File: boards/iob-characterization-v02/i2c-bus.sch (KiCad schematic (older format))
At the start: 14 parts, among them U13 24LC16BT, U14 PCA9306, U15 MCP4726A0, U16 MCP4726A1, U17 LTC2451

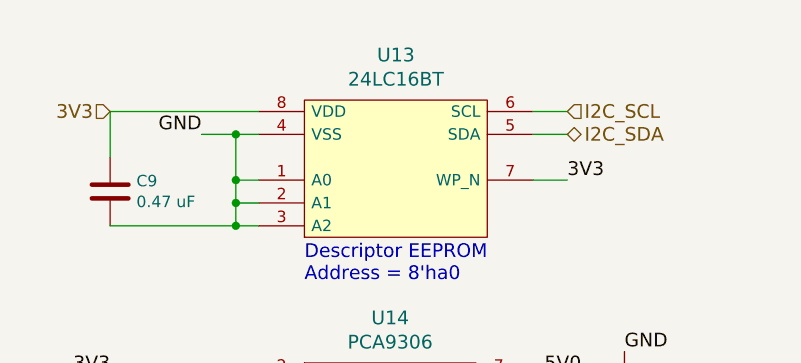
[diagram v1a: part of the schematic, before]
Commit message: Continued work on I/O characterization schematic
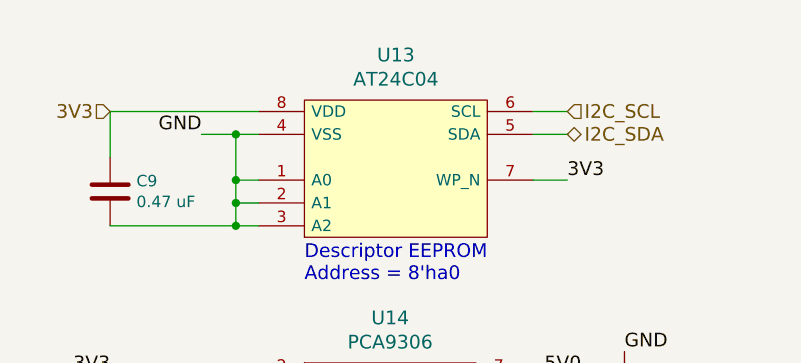
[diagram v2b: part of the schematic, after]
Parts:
- C10, C11, C13, C14, C9: footprint (none) -> azonenberg_pcb:EIA_0402_CAP_NOSILK
- R13, R14: footprint (none) -> azonenberg_pcb:EIA_0402_RES_NOSILK
- U13: value 24LC16BT -> AT24C04; footprint (none) -> azonenberg_pcb:DFN_8_0.5MM_2x3MM
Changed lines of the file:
@@
 Sheet 6 6
 Title "STARSHIPRAIDER I/O Characterization"
-Date "2018-08-10"
+Date "2018-08-13"
 Rev "0.2"
 Comp "Andrew D. Zonenberg"
@@
 AR Path="/5B92BCA2/5B932A67" Ref="U13"  Part="1"
 F 0 "U13" H 3750 3497 60  0000 C CNN
-F 1 "24LC16BT" H 3750 3391 60  0000 C CNN
-F 2 "" H 3750 3000 60  0001 C CNN
+F 1 "AT24C04" H 3750 3391 60  0000 C CNN
+F 2 "azonenberg_pcb:DFN_8_0.5MM_2x3MM" H 3750 3000 60  0001 C CNN
 F 3 "" H 3750 3000 60  0000 C CNN
 	1    3350 2700
@@
 F 0 "C9" H 2615 2546 50  0000 L CNN
 F 1 "0.47 uF" H 2615 2455 50  0000 L CNN
-F 2 "" H 2538 2350 50  0001 C CNN
+F 2 "azonenberg_pcb:EIA_0402_CAP_NOSILK" H 2538 2350 50  0001 C CNN
 F 3 "" H 2500 2500 50  0000 C CNN
 	1    2500 2500
@@
 F 0 "C11" H 4865 3396 50  0000 L CNN
 F 1 "0.47 uF" H 4865 3305 50  0000 L CNN
-F 2 "" H 4788 3200 50  0001 C CNN
+F 2 "azonenberg_pcb:EIA_0402_CAP_NOSILK" H 4788 3200 50  0001 C CNN
 F 3 "" H 4750 3350 50  0000 C CNN
 	1    4750 3350
@@
 F 0 "C10" H 2615 3496 50  0000 L CNN
 F 1 "0.47 uF" H 2615 3405 50  0000 L CNN
-F 2 "" H 2538 3300 50  0001 C CNN
+F 2 "azonenberg_pcb:EIA_0402_CAP_NOSILK" H 2538 3300 50  0001 C CNN
 F 3 "" H 2500 3450 50  0000 C CNN
 	1    2500 3450
@@
 F 0 "C13" H 7465 2346 50  0000 L CNN
 F 1 "0.47 uF" H 7465 2255 50  0000 L CNN
-F 2 "" H 7388 2150 50  0001 C CNN
+F 2 "azonenberg_pcb:EIA_0402_CAP_NOSILK" H 7388 2150 50  0001 C CNN
 F 3 "" H 7350 2300 50  0000 C CNN
 	1    7350 2300
@@
 F 0 "R13" H 5470 3596 50  0000 L CNN
 F 1 "4.7K" V 5400 3450 50  0000 L CNN
-F 2 "" V 5330 3550 50  0001 C CNN
+F 2 "azonenberg_pcb:EIA_0402_RES_NOSILK" V 5330 3550 50  0001 C CNN
 F 3 "" H 5400 3550 50  0000 C CNN
 	1    5400 3550
@@
 F 0 "R14" H 5770 3696 50  0000 L CNN
 F 1 "4.7K" V 5700 3550 50  0000 L CNN
-F 2 "" V 5630 3650 50  0001 C CNN
+F 2 "azonenberg_pcb:EIA_0402_RES_NOSILK" V 5630 3650 50  0001 C CNN
 F 3 "" H 5700 3650 50  0000 C CNN
 	1    5700 3650
@@
 F 0 "C14" H 7465 3796 50  0000 L CNN
 F 1 "0.47 uF" H 7465 3705 50  0000 L CNN
-F 2 "" H 7388 3600 50  0001 C CNN
+F 2 "azonenberg_pcb:EIA_0402_CAP_NOSILK" H 7388 3600 50  0001 C CNN
 F 3 "" H 7350 3750 50  0000 C CNN
 	1    7350 3750

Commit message: Continued initial routing of IOB characterization board
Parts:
- C12: footprint (none) -> azonenberg_pcb:EIA_0805_CAP_NOSILK
- C15: footprint (none) -> azonenberg_pcb:EIA_0402_CAP_NOSILK
- U14: footprint (none) -> azonenberg_pcb:DFN_8_0.35MM_1x1.4MM
- U15, U16: footprint (none) -> azonenberg_pcb:SOT23_6
- U17: footprint (none) -> azonenberg_pcb:DFN_8_0.5MM_2x3MM
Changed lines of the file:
@@
 Sheet 6 6
 Title "STARSHIPRAIDER I/O Characterization"
-Date "2018-08-13"
+Date "2018-08-15"
 Rev "0.2"
 Comp "Andrew D. Zonenberg"
@@
 F 0 "U14" H 3725 4647 60  0000 C CNN
 F 1 "PCA9306" H 3725 4541 60  0000 C CNN
-F 2 "" H 3600 3850 60  0001 C CNN
+F 2 "azonenberg_pcb:DFN_8_0.35MM_1x1.4MM" H 3600 3850 60  0001 C CNN
 F 3 "" H 3600 3850 60  0001 C CNN
 	1    3350 3850
@@
 F 0 "U17" H 8650 6597 60  0000 C CNN
 F 1 "LTC2451" H 8650 6491 60  0000 C CNN
-F 2 "" H 8250 5700 60  0001 C CNN
+F 2 "azonenberg_pcb:DFN_8_0.5MM_2x3MM" H 8250 5700 60  0001 C CNN
 F 3 "" H 8250 5700 60  0001 C CNN
 	1    8250 5700
@@
 F 0 "C15" H 7465 5246 50  0000 L CNN
 F 1 "0.1 uF" H 7465 5155 50  0000 L CNN
-F 2 "" H 7388 5050 50  0001 C CNN
+F 2 "azonenberg_pcb:EIA_0402_CAP_NOSILK" H 7388 5050 50  0001 C CNN
 F 3 "" H 7350 5200 50  0000 C CNN
 	1    7350 5200
@@
 F 0 "C12" H 6965 5246 50  0000 L CNN
 F 1 "10 uF" H 6965 5155 50  0000 L CNN
-F 2 "" H 6888 5050 50  0001 C CNN
+F 2 "azonenberg_pcb:EIA_0805_CAP_NOSILK" H 6888 5050 50  0001 C CNN
 F 3 "" H 6850 5200 50  0000 C CNN
 	1    6850 5200
@@
 F 0 "U15" H 8575 3797 60  0000 C CNN
 F 1 "MCP4726A0" H 8575 3691 60  0000 C CNN
-F 2 "" H 8200 2550 60  0001 C CNN
+F 2 "azonenberg_pcb:SOT23_6" H 8200 2550 60  0001 C CNN
 F 3 "" H 8200 2550 60  0001 C CNN
 	1    8250 2800
@@
 F 0 "U16" H 8575 5247 60  0000 C CNN
 F 1 "MCP4726A1" H 8575 5141 60  0000 C CNN
-F 2 "" H 8200 4000 60  0001 C CNN
+F 2 "azonenberg_pcb:SOT23_6" H 8200 4000 60  0001 C CNN
 F 3 "" H 8200 4000 60  0001 C CNN
 	1    8250 4250
